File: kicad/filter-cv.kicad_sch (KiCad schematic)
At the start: 21 parts, among them Q10 2N3904, Q11 2N3906, Q9 2N3906, U16 TL074

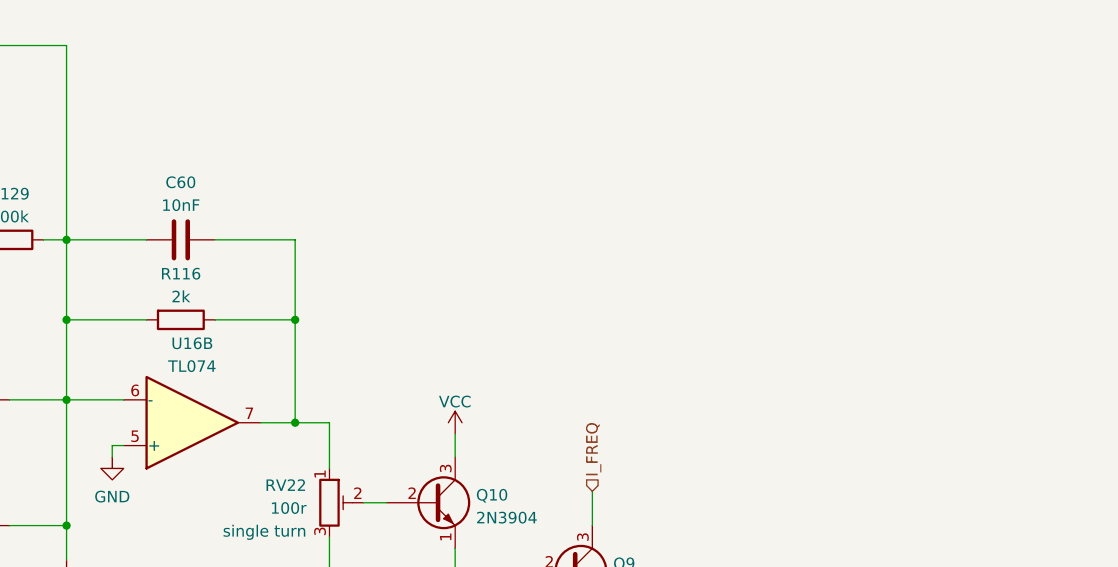
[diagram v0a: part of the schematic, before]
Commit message: Minor tweaks to rev2 values
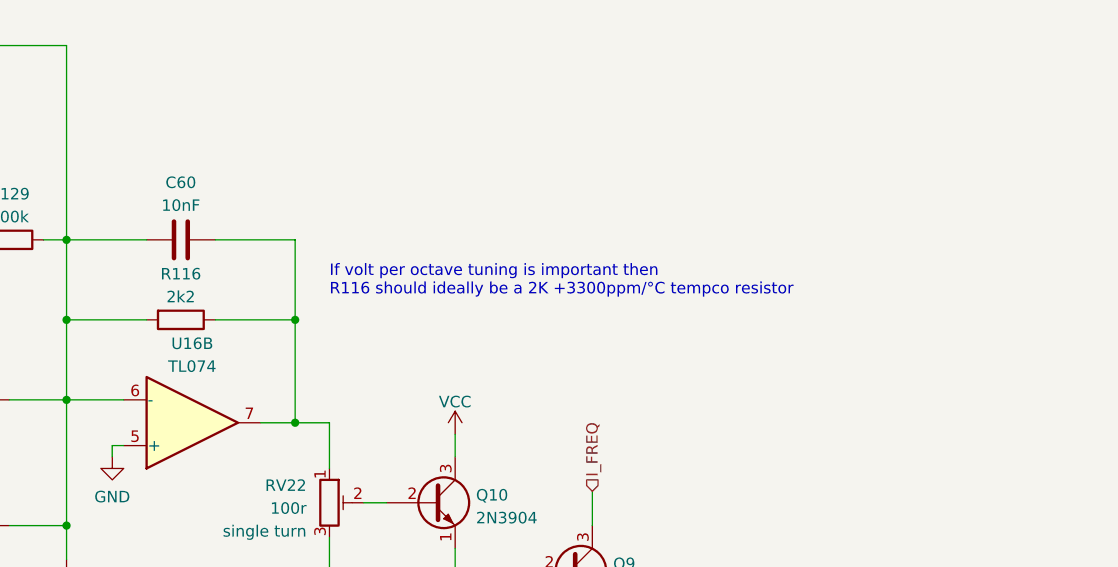
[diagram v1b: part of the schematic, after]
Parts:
- R116: value 2k -> 2k2
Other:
- note added: "If volt per octave tuning is important then R116 should ideally be a 2K +3300ppm/°C tempco resistor"
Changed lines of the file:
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@@
     (stroke (width 0) (type default))
+  )
+  (text "If volt per octave tuning is important then\nR116 should ideally be a 2K +3300ppm/°C tempco resistor"
+    (at 106.68 128.27 0)
+    (effects (font (size 1.27 1.27)) (justify left bottom))
   )
   (hierarchical_label "RES_CV_ATTV_BOTTOM" (shape input) (at 43.18 50.8 180) (fields_autoplaced)
@@
       (effects (font (size 1.27 1.27)))
     )
-    (property "Value" "2k" (at 90.17 128.27 90)
-      (effects (font (size 1.27 1.27)))
-    )
+    (property "Value" "2k2" (at 90.17 128.27 90)
+      (effects (font (size 1.27 1.27)))
+    )

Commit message: Changing decoupling caps to ceramic X7R
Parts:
- C59, C65: Spec ceramic C0G -> ceramic X7R
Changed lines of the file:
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@@
       (effects (font (size 1.27 1.27)) hide)
     )
-    (property "Spec" "ceramic C0G" (at 195.58 64.77 90)
+    (property "Spec" "ceramic X7R" (at 195.58 64.77 90)
       (effects (font (size 1.27 1.27)) hide)
     )
@@
       (effects (font (size 1.27 1.27)) hide)
     )
-    (property "Spec" "ceramic C0G" (at 195.58 77.47 90)
-      (effects (font (size 1.27 1.27)) hide)
-    )
+    (property "Spec" "ceramic X7R" (at 195.58 77.47 90)
+      (effects (font (size 1.27 1.27)) hide)
+    )

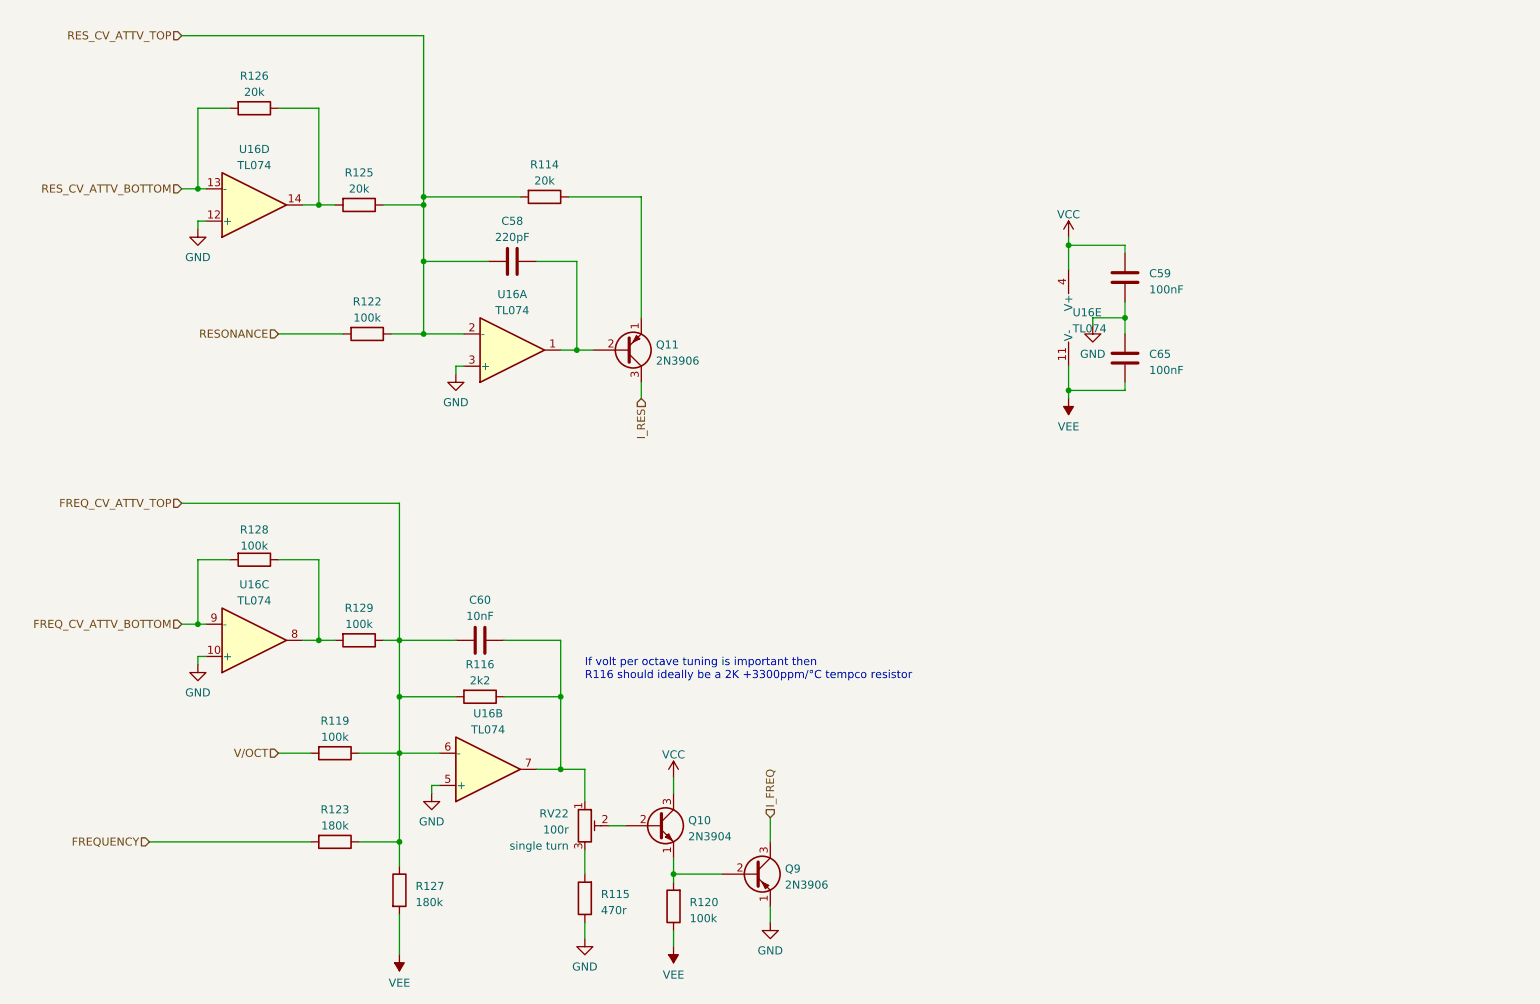
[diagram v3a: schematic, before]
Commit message: Updating board for new footprint libraries
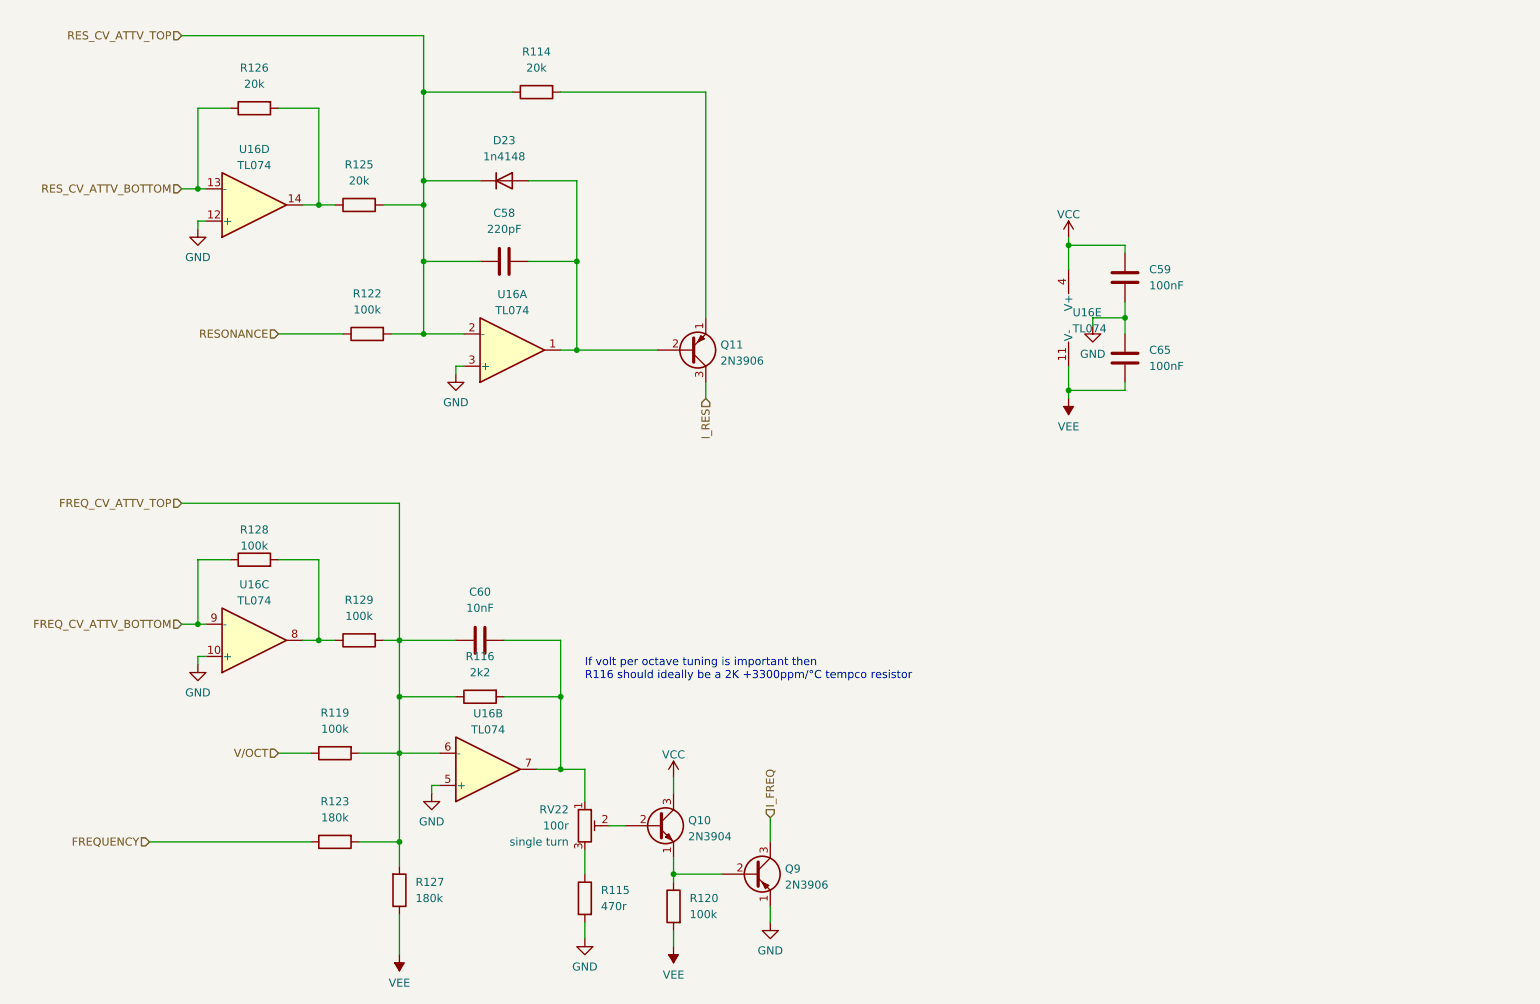
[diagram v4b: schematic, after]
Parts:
- added D23: 1n4148, Rumblesan_Standard_Parts:D_DO-35_SOD27_P7.62mm_Horizontal, symbol Device:D
- C58, C59, C60, C65: symbol Rumblesan Standard Parts:C -> Rumblesan_Standard_Parts:C
- Q10, Q11, Q9: footprint Rumblesan_Standard_Parts:TO-92_Inline_Wide -> Package_TO_SOT_THT:TO-92_Inline_Wide
- R114, R115, R116, R119, R120, R122, R123, R125, R126, R127, R128, R129: symbol Rumblesan Standard Parts:R -> Rumblesan_Standard_Parts:R
- RV22: footprint Rumblesan_Standard_Parts:Potentiometer_THT_Bourns_3306P_Vertical -> Rumblesan_Potentiometer_THT:Potentiometer_THT_Bourns_3306P_Vertical; symbol Rumblesan Standard Parts:R_Potentiometer_Trim -> Rumblesan_Standard_Parts:R_Potentiometer_Trim
- U16: footprint Rumblesan_Standard_Parts:DIP-14_W7.62mm_Socket -> Package_DIP:DIP-14_W7.62mm_Socket
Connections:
- net RES_CV_ATTV_TOP: now also D23.1 (K)
- net at C58.2, Q11.2 (B), U16.1: now also D23.2 (A)
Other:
- moved on the sheet: C58, Q11, R114, R115, R116, R119, R120, R122, R123, R125, R126, R127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

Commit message: Tweaking filter resonance control circuitry
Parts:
- added D24: 1n4148, Rumblesan_Standard_Parts:D_DO-35_SOD27_P7.62mm_Horizontal, symbol Device:D
- added R131: 10k, Rumblesan_Standard_Parts:R_Axial_DIN0207_L6.3mm_D2.5mm_P10.16mm_Horizontal, symbol Rumblesan_Standard_Parts:R
- added R132: 4k7, Rumblesan_Standard_Parts:R_Axial_DIN0207_L6.3mm_D2.5mm_P10.16mm_Horizontal, symbol Rumblesan_Standard_Parts:R
- added R133: 1m, Rumblesan_Standard_Parts:R_Axial_DIN0207_L6.3mm_D2.5mm_P10.16mm_Horizontal, symbol Rumblesan_Standard_Parts:R
- R114: value 20k -> 100k
- R122: value 100k -> 330k
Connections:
- net GND: now also R131.1, R132.1
- net RES_CV_ATTV_TOP: now also R133.1
- net VCC: now also R133.2
- net at Q11.1 (E), R114.1: now also D24.1 (K), R131.2
- new net: D24.2 (A), R132.2

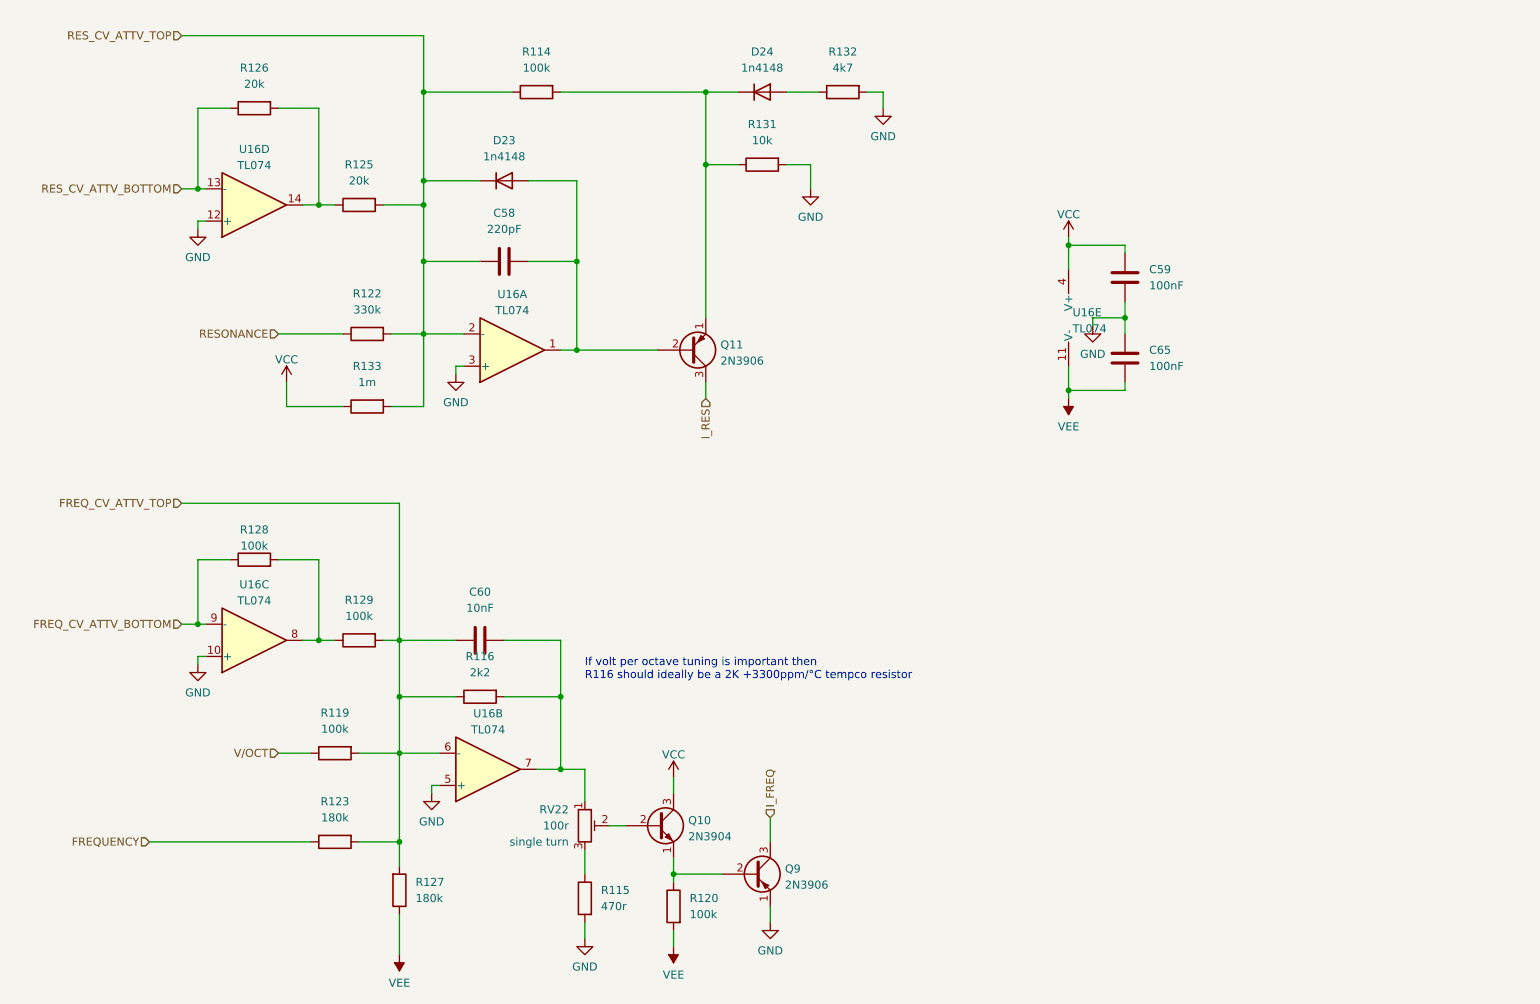
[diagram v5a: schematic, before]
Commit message: Updating with rev03 changes
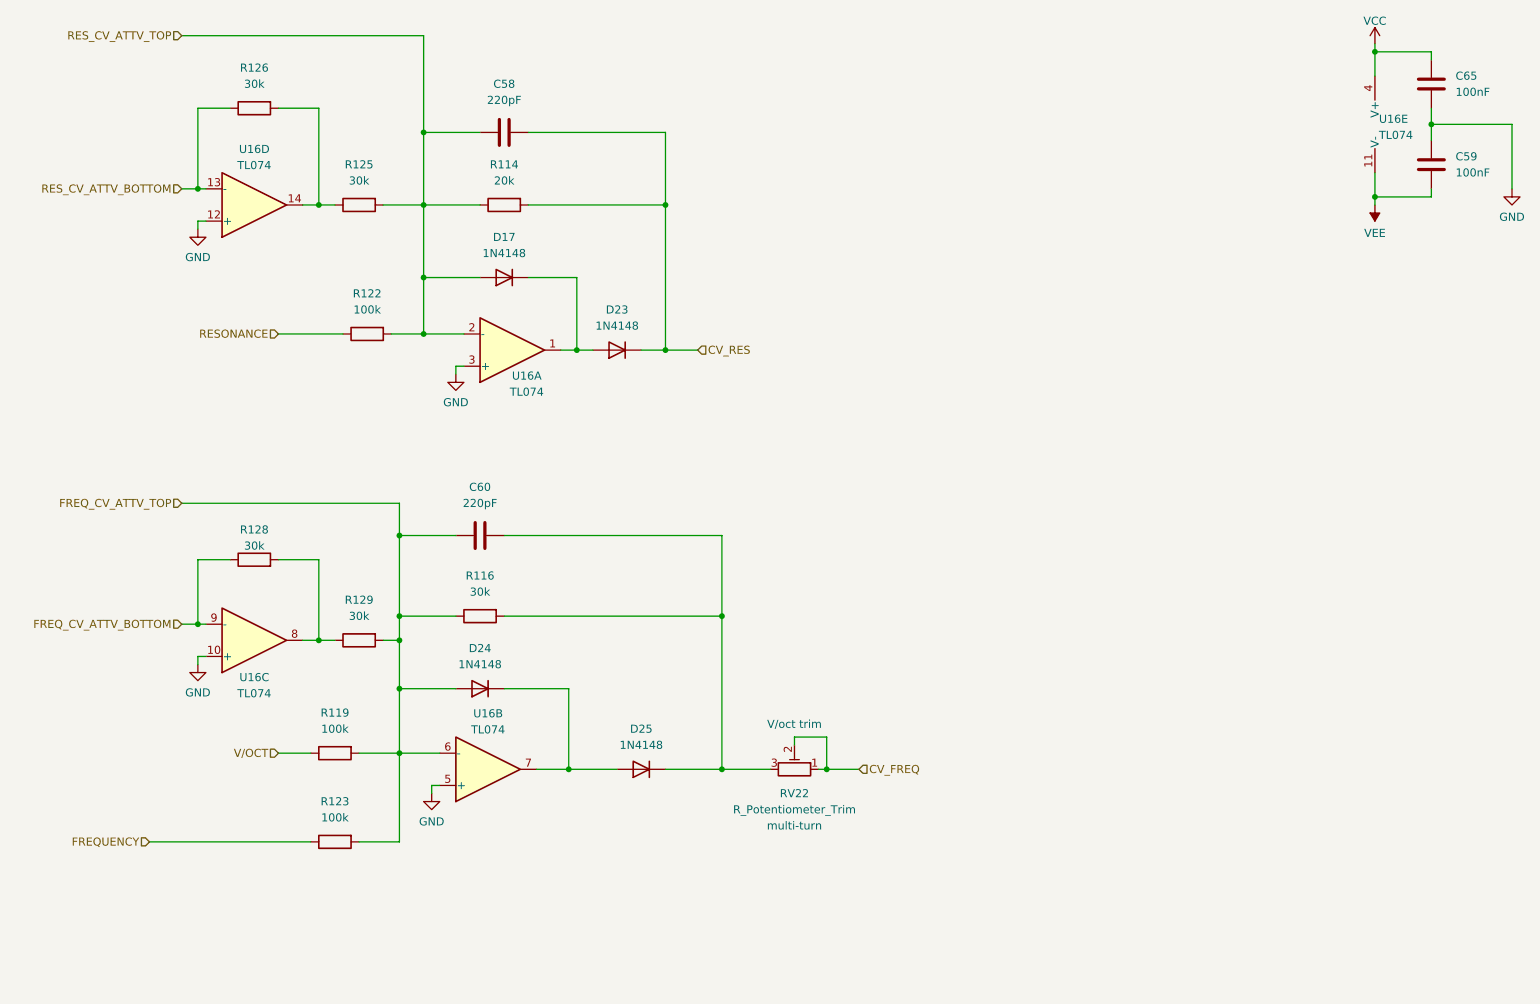
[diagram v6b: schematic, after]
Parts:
- removed D23, D24: 1n4148, Rumblesan_Standard_Parts:D_DO-35_SOD27_P7.62mm_Horizontal, symbol Device:D
- removed Q10: 2N3904, Package_TO_SOT_THT:TO-92_Inline_Wide, symbol Transistor_BJT:2N3904
- removed Q11, Q9: 2N3906, Package_TO_SOT_THT:TO-92_Inline_Wide, symbol Transistor_BJT:2N3906
- removed R115: 470r, Rumblesan_Standard_Parts:R_Axial_DIN0207_L6.3mm_D2.5mm_P10.16mm_Horizontal, symbol Rumblesan_Standard_Parts:R
- removed R120: 100k, Rumblesan_Standard_Parts:R_Axial_DIN0207_L6.3mm_D2.5mm_P10.16mm_Horizontal, symbol Rumblesan_Standard_Parts:R
- removed R127: 180k, Rumblesan_Standard_Parts:R_Axial_DIN0207_L6.3mm_D2.5mm_P10.16mm_Horizontal, symbol Rumblesan_Standard_Parts:R
- removed R131: 10k, Rumblesan_Standard_Parts:R_Axial_DIN0207_L6.3mm_D2.5mm_P10.16mm_Horizontal, symbol Rumblesan_Standard_Parts:R
- removed R132: 4k7, Rumblesan_Standard_Parts:R_Axial_DIN0207_L6.3mm_D2.5mm_P10.16mm_Horizontal, symbol Rumblesan_Standard_Parts:R
- removed R133: 1m, Rumblesan_Standard_Parts:R_Axial_DIN0207_L6.3mm_D2.5mm_P10.16mm_Horizontal, symbol Rumblesan_Standard_Parts:R
- added D17, D23, D24, D25: 1N4148, Diode_THT:D_DO-35_SOD27_P7.62mm_Horizontal, symbol Diode:1N4148
- C60: value 10nF -> 220pF
- R114: value 100k -> 20k
- R116: value 2k2 -> 30k
- R122: value 330k -> 100k
- R123: value 180k -> 100k
- R125, R126: value 20k -> 30k
- R128, R129: value 100k -> 30k
- RV22: value 100r -> R_Potentiometer_Trim; Name (none) -> V/oct trim; Spec single turn -> multi-turn
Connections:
- net FREQ_CV_ATTV_TOP: now also D24.2 (A)
- net GND: now also C65.2; no longer C65.1
- net RES_CV_ATTV_TOP: now also D17.2 (A)
- net VCC: now also C65.1; no longer C59.1
- net VEE: now also C59.1; no longer C65.2
- net at RV22.3: now also C60.2, R116.1, D25.1 (K)
- net CV_FREQ: now reaches RV22.2
- net CV_FREQ: now also RV22.1
- net CV_RES: now reaches R114.1
- net CV_RES: now also C58.2, D23.1 (K)
- net at U16.1: now also D17.1 (K), D23.2 (A); no longer C58.2
- new net: D24.1 (K), D25.2 (A), U16.7
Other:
- note removed: "If volt per octave tuning is important then R116 should ideally be a 2K +3300ppm/°C tempco resistor"
- moved on the sheet: C58, C59, C60, C65, R116, U16E
